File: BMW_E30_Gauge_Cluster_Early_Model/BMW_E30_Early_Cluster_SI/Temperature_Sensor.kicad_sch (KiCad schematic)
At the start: 42 parts, among them K1 Relay_SPDT, Q11 BC337-25, Q2 BC547B, U2 LM2901

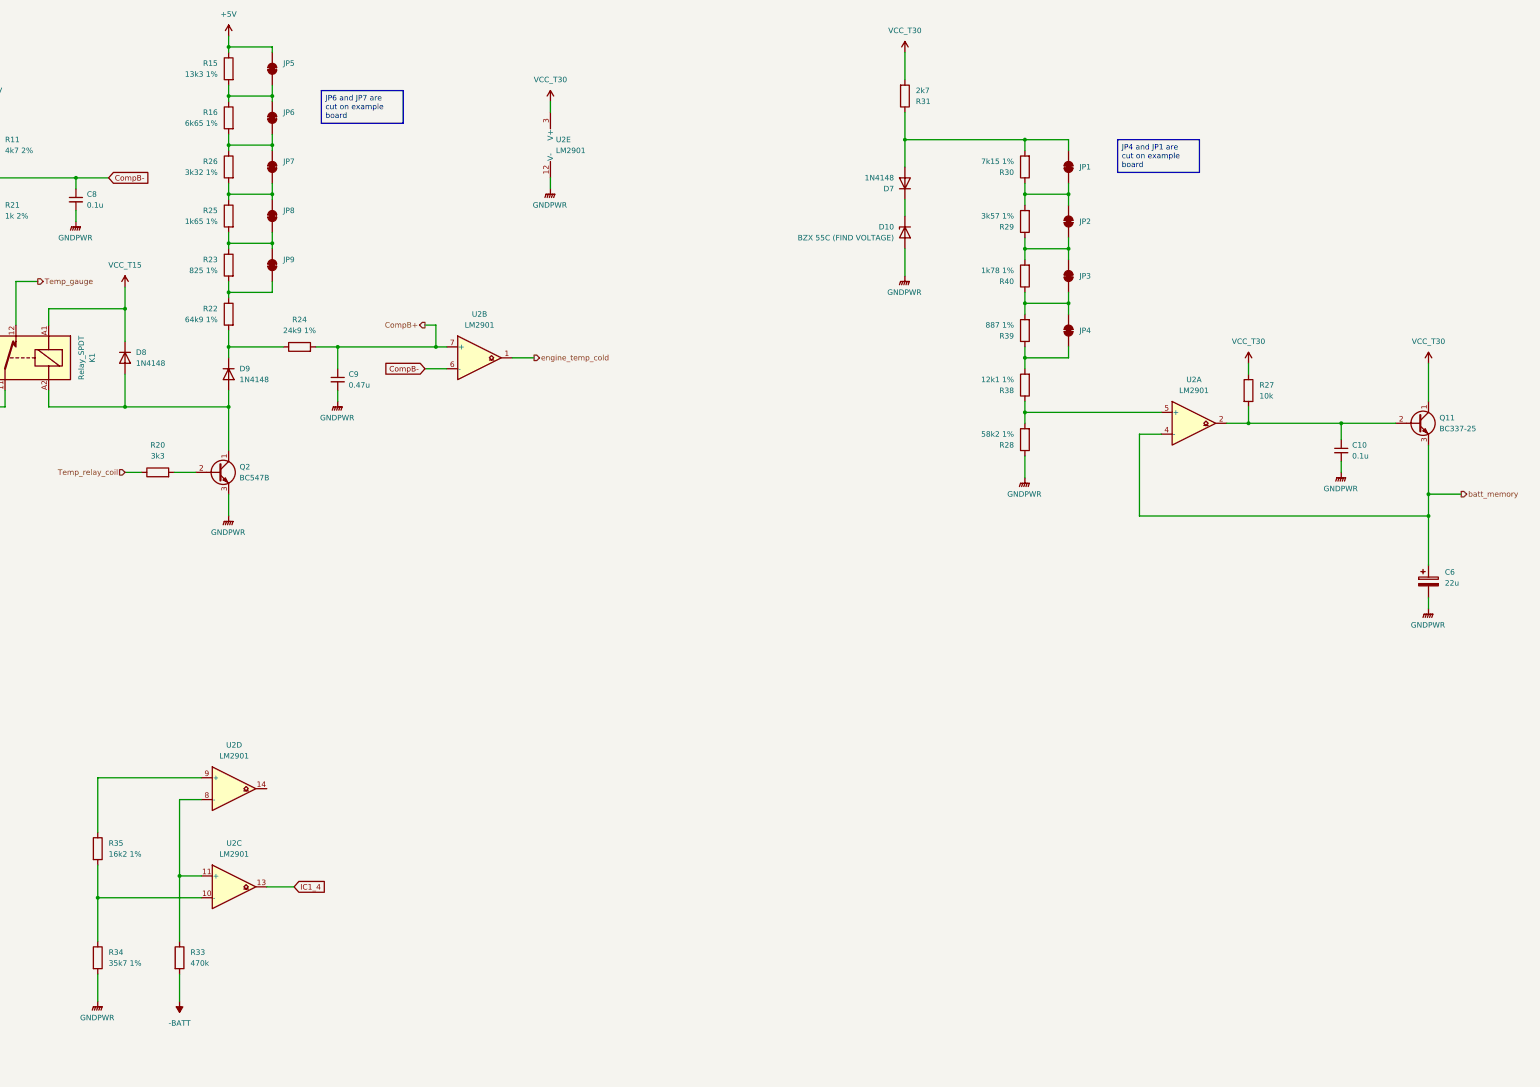
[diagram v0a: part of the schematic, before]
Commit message: Updates to Comparator Circuit
Updated Comparator circuit and the final pins of the MCU. Majority of signals and components are accounted for. Next step is footprint assignment and then double checking each component.
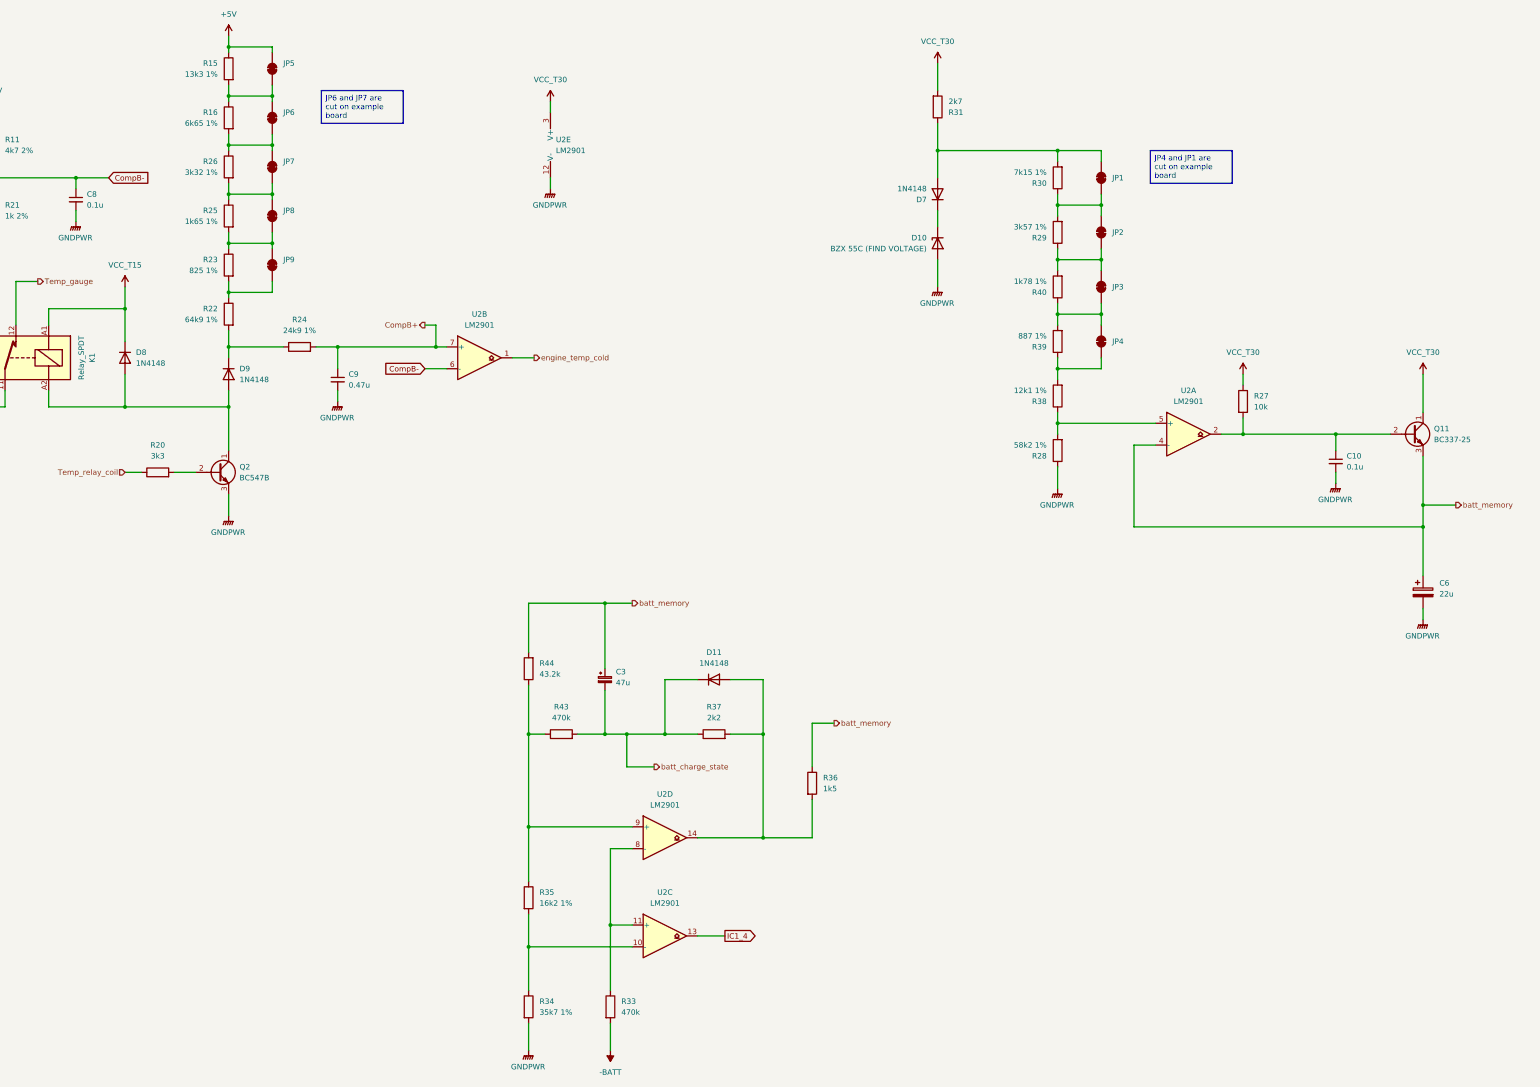
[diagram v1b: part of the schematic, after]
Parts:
- added C3: 47u, symbol Device:C_Polarized_Small
- added D11: 1N4148, Diode_THT:D_DO-35_SOD27_P7.62mm_Horizontal, symbol Diode:1N4148
- added R36: 1k5, symbol Device:R
- added R37: 2k2, symbol Device:R
- added R43: 470k, symbol Device:R
- added R44: 43.2k, symbol Device:R
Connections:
- net batt_memory: now also C3.1, R36.1, R44.2
- net at U2.14: now also D11.2 (A), R36.2, R37.2
- net at R35.1, U2.9 (+): now also R43.1, R44.1
- new net batt_charge_state: C3.2, D11.1 (K), R37.1, R43.2
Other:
- moved on the sheet: C10, C6, D10, D7, JP1, JP2, JP3, JP4, Q11, R27, R28, R29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
